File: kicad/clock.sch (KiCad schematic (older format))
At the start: 43 parts, among them U1 4060, U2 4027, Y1 32768

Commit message: Finished rough schematic
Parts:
- removed U1: 4060, symbol 4060
- removed U2: 4027, symbol 4027
- added U2: CD4060, symbol clock:CD4060
- added U6: 4027, symbol 4xxx_IEEE:4027
- C1, C2: symbol C -> Device:C
- Q1, Q2, Q3, Q4, Q5, Q6: renamed from Q?; symbol PN2222A -> clock-rescue:PN2222A
- R1, R2: symbol R -> Device:R
- R10, R11, R12, R13, R14, R15, R3, R4, R5, R6, R7, R8, R9: renamed from R?; symbol R -> Device:R
- U1, U12, U9: renamed from U?; symbol 74LS390 -> clock-rescue:74LS390
- U10, U13, U3, U7: renamed from U?; symbol 4543 -> clock-rescue:4543
- U11, U14, U5, U8: renamed from U?; symbol 7SEGMENT_CC -> clock-rescue:7SEGMENT_CC
- U4: renamed from U?; symbol 74HC04 -> clock-rescue:74HC04
- Y1: symbol Crystal -> Device:Crystal
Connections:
- wire segments 93 -> 98

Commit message: Fixed and prettied schematic
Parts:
- removed U1, U12, U9: 74HC390, symbol clock-rescue:74LS390
- removed U4: 74HC04, symbol clock-rescue:74HC04
- removed U6: 4027, symbol 4xxx_IEEE:4027
- added R2, R3, R4, R5, R6: 1M, symbol Device:R
- added U1: 74HC04, symbol 74xx:74HC04
- added U2, U7, U8: 74LS390, symbol 74xx:74LS390
- added U6: 4027, symbol 4xxx:4027
- R1: value 10M -> 1M
- renumbered R5 to R10, R6 to R11, R7 to R12, R8 to R13, R9 to R14, R10 to R15, R11 to R16, R12 to R17, R13 to R18, R14 to R19, R15 to R20, R2 to R7, R3 to R8, R4 to R9, U8 to U10, U10 to U11, U11 to U12, U2 to U3, U3 to U4, U7 to U9
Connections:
- net labels added: Q0, Q1, Q2, Q3, R0, R1, R2, R3, S0, S1, S2, S3, T0, T1, T2, T3
- wire segments 98 -> 150
- no-connect marks 5 -> 15
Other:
- moved on the sheet: C1, Q3, Q4, R14, R15, R18, Y1

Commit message: Some grouping
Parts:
- C1, C2: footprint (none) -> Capacitors_THT:C_Rect_L4.0mm_W2.5mm_P2.50mm
- R1, R10, R11, R12, R13, R14, R15, R16, R17, R18, R19, R2, R20, R3, R4, R5, R6, R7, R8, R9: footprint (none) -> Resistors_THT:R_Axial_DIN0207_L6.3mm_D2.5mm_P10.16mm_Horizontal
- U1: footprint (none) -> Housings_DIP:DIP-14_W7.62mm
- U10, U12, U14, U5: footprint (none) -> Displays_7-Segment:HDSP-78xx
- U11, U13, U2, U3, U4, U6, U7, U8, U9: footprint (none) -> Housings_DIP:DIP-16_W7.62mm
- Y1: footprint (none) -> Crystals:Crystal_DS26_d2.0mm_l6.0mm_Vertical

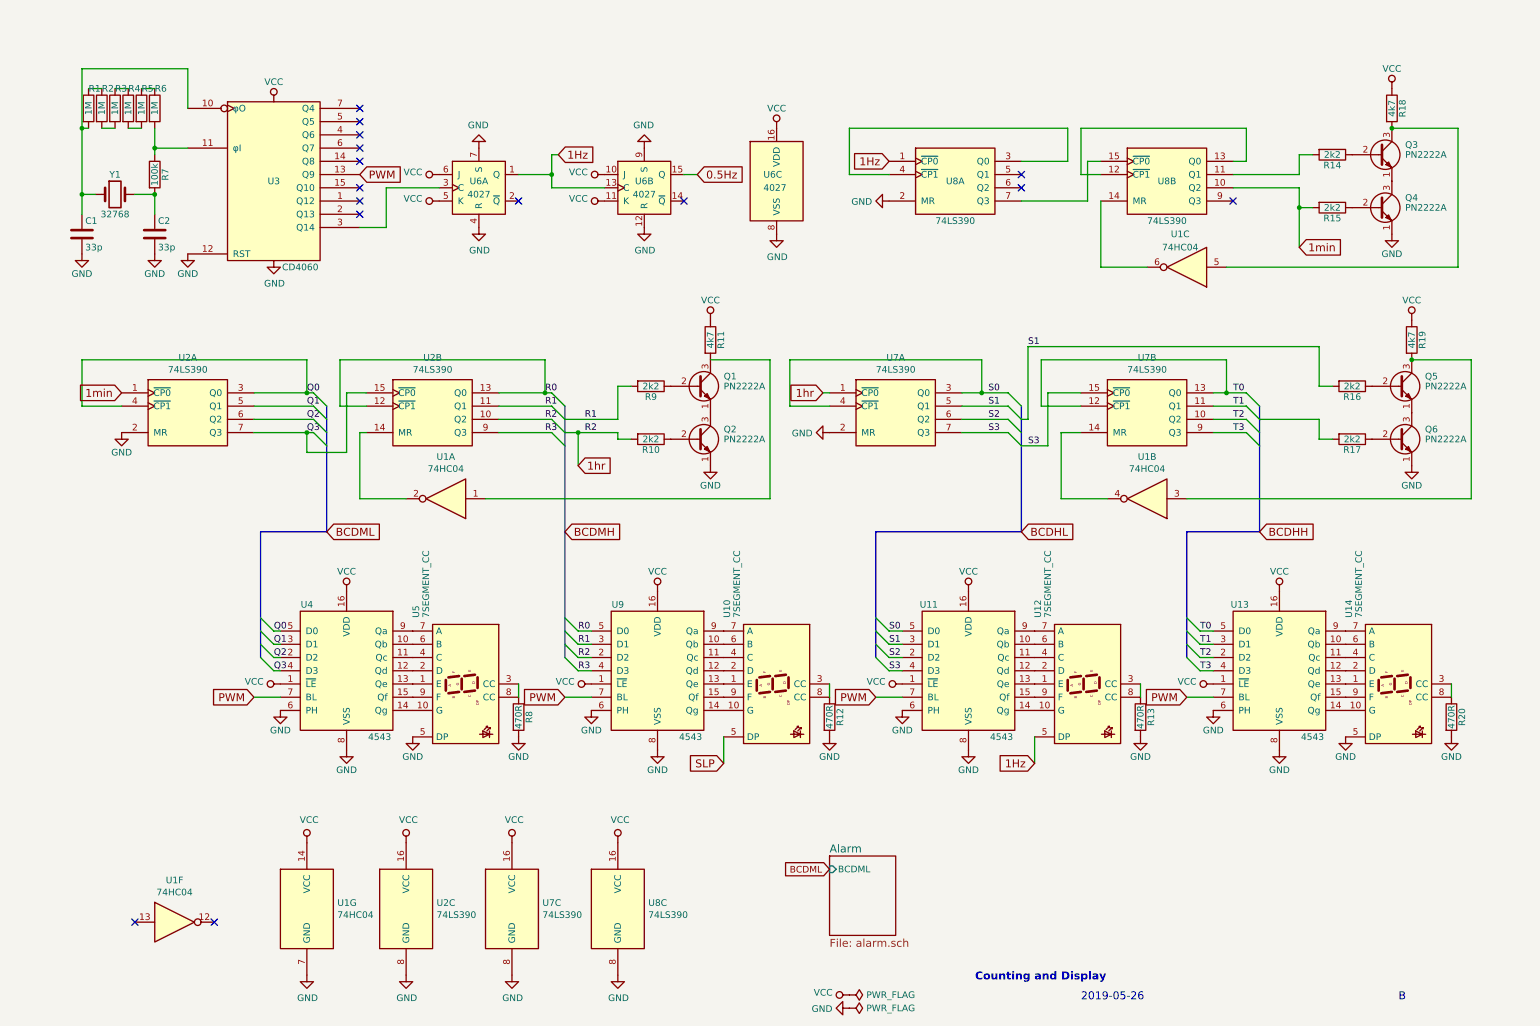
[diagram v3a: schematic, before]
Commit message: Fixed buses between sheets; comparator BCD inputs connected
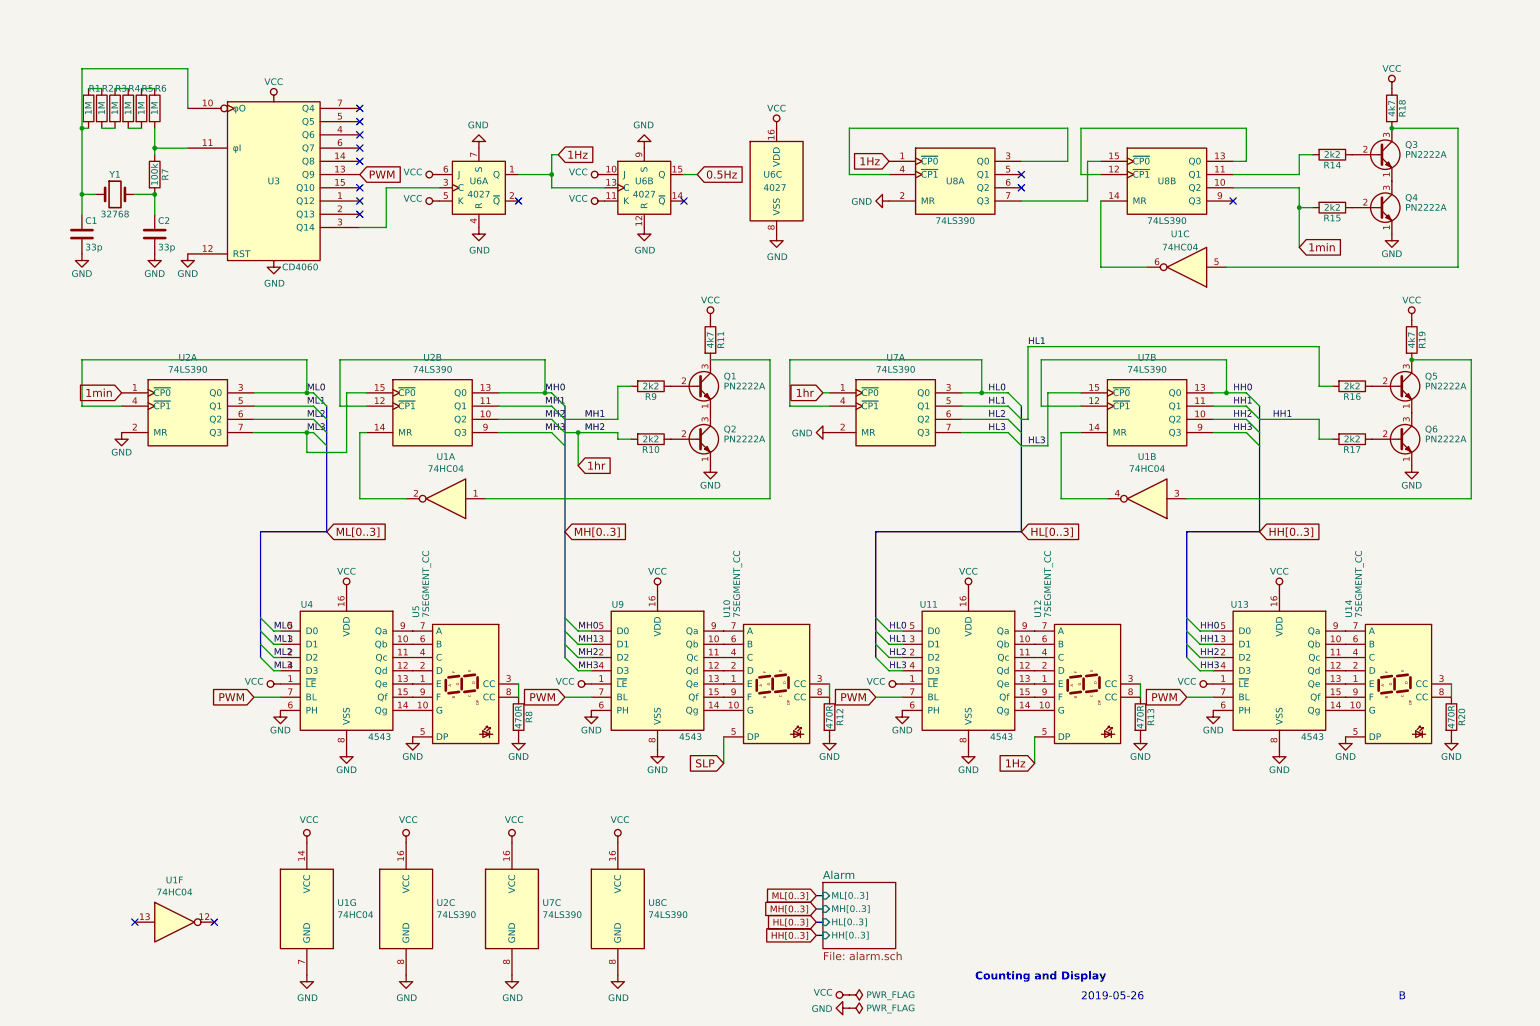
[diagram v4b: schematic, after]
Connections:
- net T1 is gone; now on net HH1: U13.3 (D1), U7.11 (Q1)
- net HH1: now reaches R17.2
- net Q0 renamed ML0
- net Q1 renamed ML1
- net Q2 renamed ML2
- net Q3 renamed ML3
- net R0 renamed MH0
- net R1 renamed MH1
- net R3 renamed MH3
- net S0 renamed HL0
- net S1 renamed HL1
- net S2 renamed HL2
- net S3 renamed HL3
- net T0 renamed HH0
- net T2 renamed HH2
- net T3 renamed HH3
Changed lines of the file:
@@
 	8950 4750 9050 4850
 Text GLabel 2450 4100 2    60   Input ~ 0
-BCDML
+ML[0..3]
 Text GLabel 4250 4100 2    60   Input ~ 0
-BCDMH
+MH[0..3]
 Text GLabel 7700 4100 2    60   Input ~ 0
-BCDHL
+HL[0..3]
 Text GLabel 9500 4100 2    60   Input ~ 0
-BCDHH
+HH[0..3]
 $Sheet
-S 6250 6550 500  600
+S 6200 6750 550  500
 U 5CED0B3E
 F0 "Alarm" 60
 F1 "alarm.sch" 60
-F2 "BCDML" I L 6250 6650 50
+F2 "ML[0..3]" I L 6200 6850 50
+F3 "MH[0..3]" I L 6200 6950 50
+F4 "HH[0..3]" I L 6200 7150 50
+F5 "HL[0..3]" I L 6200 7050 50
 $EndSheet
 $Comp
@@
 	2300 3050 2300 2800
 Text Label 2300 3050 0    50   ~ 0
-Q0
+ML0
 Text Label 2300 3150 0    50   ~ 0
-Q1
+ML1
 Text Label 2300 3250 0    50   ~ 0
-Q2
+ML2
 Text Label 2300 3350 0    50   ~ 0
-Q3
+ML3
 Wire Wire Line
 	2050 4850 2100 4850
@@
 	2100 5150 2050 5150
 Text Label 2050 4850 0    50   ~ 0
-Q0
+ML0
 Text Label 2050 4950 0    50   ~ 0
-Q1
+ML1
 Text Label 2050 5050 0    50   ~ 0
-Q2
+ML2
 Text Label 2050 5150 0    50   ~ 0
-Q3
+ML3
 Wire Wire Line
 	4100 3050 4150 3050
@@
 	4100 2800 2550 2800
 Text Label 4100 3050 0    50   ~ 0
-R0
+MH0
 Text Label 4100 3150 0    50   ~ 0
-R1
+MH1
 Text Label 4100 3250 0    50   ~ 0
-R2
+MH2
 Text Label 4100 3350 0    50   ~ 0
-R3
+MH3
 Wire Wire Line
 	4450 4850 4350 4850
@@
 	4350 5150 4450 5150
 Text Label 4350 4850 0    50   ~ 0
-R0
+MH0
 Text Label 4350 4950 0    50   ~ 0
-R1
+MH1
 Text Label 4350 5050 0    50   ~ 0
-R2
+MH2
 Text Label 4350 5150 0    50   ~ 0
-R3
+MH3
 Text Label 4400 3250 0    50   ~ 0
-R1
+MH1
 Text Label 4400 3350 0    50   ~ 0
-R2
+MH2
 Wire Wire Line
 	4150 1250 4150 1400
@@
 	7400 2800 5950 2800
 Text Label 7450 3050 0    50   ~ 0
-S0
+HL0
 Text Label 7450 3150 0    50   ~ 0
-S1
+HL1
 Text Label 7450 3250 0    50   ~ 0
-S2
+HL2
 Text Label 7450 3350 0    50   ~ 0
-S3
+HL3
 Text Label 7750 2700 0    50   ~ 0
-S1
+HL1
 Text Label 7750 3450 0    50   ~ 0
-S3
+HL3
 Wire Wire Line
 	6700 4850 6800 4850
@@
 	6800 5150 6700 5150
 Text Label 6700 4850 0    50   ~ 0
-S0
+HL0
 Text Label 6700 4950 0    50   ~ 0
-S1
+HL1
 Text Label 6700 5050 0    50   ~ 0
-S2
+HL2
 Text Label 6700 5150 0    50   ~ 0
-S3
+HL3
 $Comp
 L 74xx:74LS390 U7
@@
 	9250 2800 7850 2800
 Text Label 9300 3050 0    50   ~ 0
-T0
+HH0
 Text Label 9300 3150 0    50   ~ 0
-T1
+HH1
 Text Label 9300 3250 0    50   ~ 0
-T2
+HH2
 Text Label 9300 3350 0    50   ~ 0
-T3
+HH3
 Wire Wire Line
 	9050 4850 9150 4850
@@
 	9150 5150 9050 5150
 Text Label 9050 4850 0    50   ~ 0
-T0
+HH0
 Text Label 9050 4950 0    50   ~ 0
-T1
+HH1
 Text Label 9050 5050 0    50   ~ 0
-T2
+HH2
 Text Label 9050 5150 0    50   ~ 0
-T3
+HH3
 $Comp
 L 74xx:74LS390 U8
@@
 Wire Wire Line
 	600  1050 600  1550
+Text GLabel 6150 6850 0    50   Input ~ 0
+ML[0..3]
+Wire Bus Line
+	6150 6850 6200 6850
+Text Label 9600 3250 0    50   ~ 0
+HH1
+Text GLabel 6150 6950 0    50   Input ~ 0
+MH[0..3]
+Text GLabel 6150 7050 0    50   Input ~ 0
+HL[0..3]
+Text GLabel 6150 7150 0    50   Input ~ 0
+HH[0..3]
+Wire Bus Line
+	6150 6950 6200 6950
+Wire Bus Line
+	6150 7050 6200 7050
+Wire Bus Line
+	6150 7150 6200 7150
 Wire Bus Line
 	8950 4100 8950 5050
@@
 Wire Bus Line
 	4250 3150 4250 5050
-Text GLabel 6250 6650 0    50   Input ~ 0
-BCDML
 $EndSCHEMATC

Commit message: More routing, but oops displays are backwards and it's all for nothing
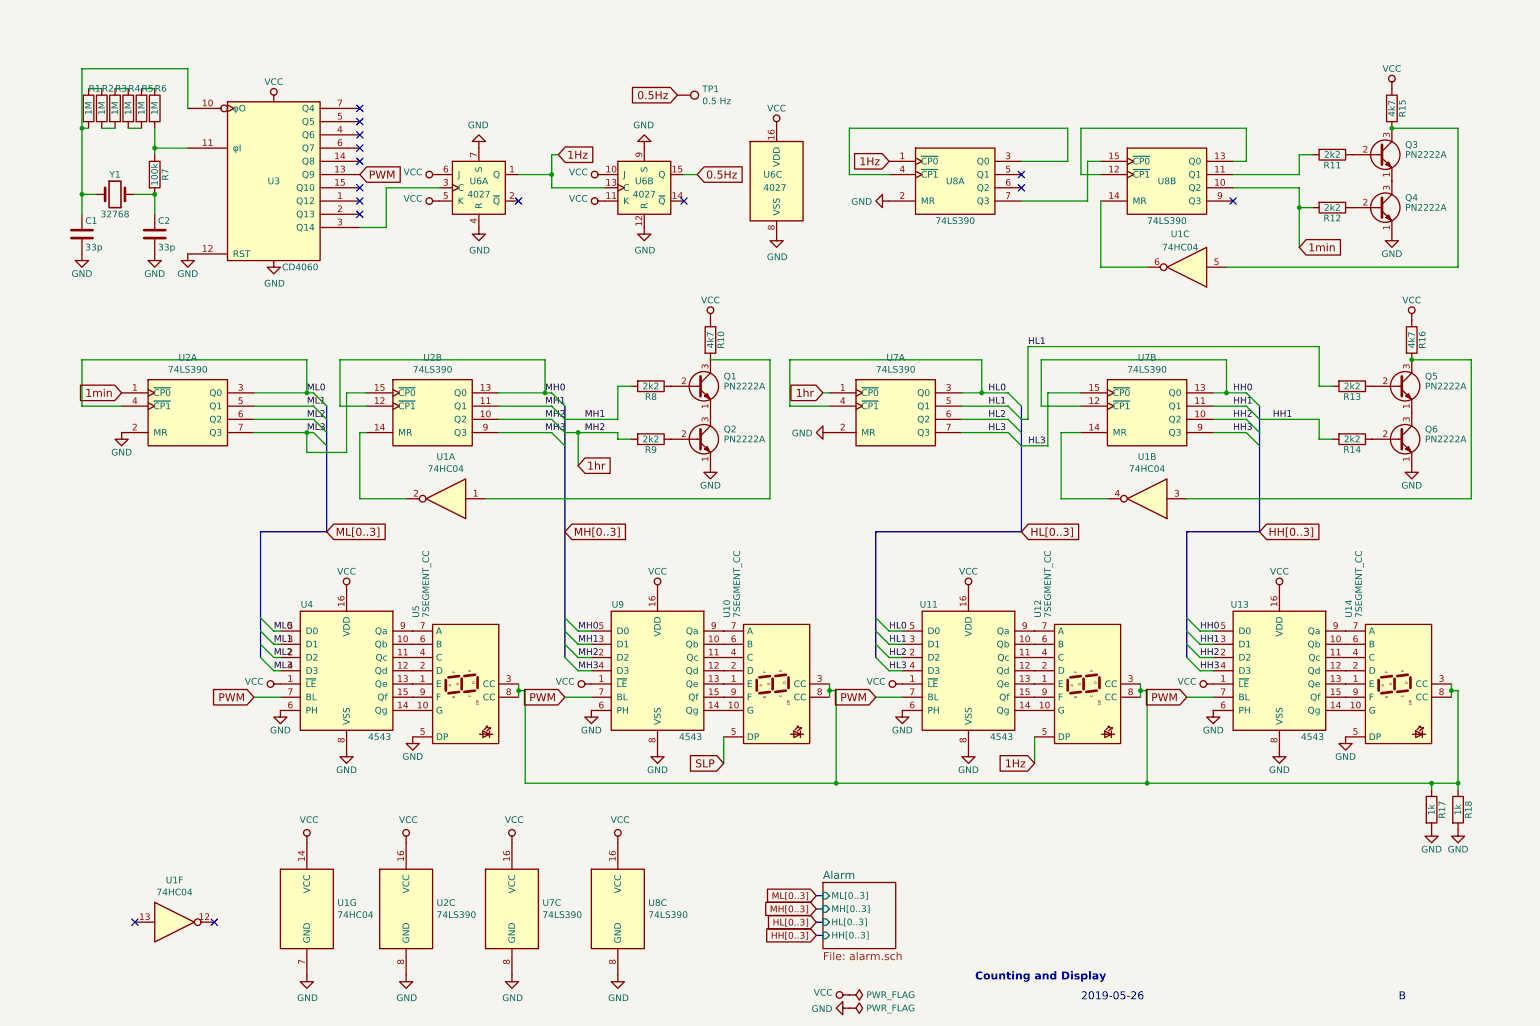
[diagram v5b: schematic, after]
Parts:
- removed R12, R13, R8: 470R, Resistors_THT:R_Axial_DIN0207_L6.3mm_D2.5mm_P10.16mm_Horizontal, symbol Device:R
- added R17: 1k, Resistors_THT:R_Axial_DIN0207_L6.3mm_D2.5mm_P10.16mm_Horizontal, symbol Device:R
- added TP1: 0.5 Hz, clock:TestPoint, symbol Connector:TestPoint
- R18: renamed from R20; value 470R -> 1k
- renumbered R11 to R10, R14 to R11, R15 to R12, R16 to R13, R17 to R14, R18 to R15, R19 to R16, R9 to R8, R10 to R9
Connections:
- net 0.5Hz: now also TP1.1
- net GND: now also R17.2
- net at U5.3 (CC), U5.8 (CC): now also R18.1, U10.3 (CC), U10.8 (CC), U12.3 (CC), U12.8 (CC), U14.3 (CC), U14.8 (CC), R17.1
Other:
- moved on the sheet: R18
